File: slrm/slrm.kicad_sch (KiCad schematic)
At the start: 8 parts, among them J1 Conn_01x07, J2 Conn_01x03, J3 Conn_01x08, U1 74HCT04, U2 74HCT574, U3 IS62C256AL-45ULI

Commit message: more schematic work, ground inputs, find the footprint for the sram
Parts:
- added C1: C_Small, symbol Device:C_Small
- added unit 4 of U1
- added unit 2 of U1
- added unit 5 of U1
- added unit 6 of U1
- added unit 7 of U1
- added unit 3 of U1
- renumbered C1 to C2, C2 to C3
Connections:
- net +5V: now also C1.1, U1.14 (VCC)
- net GND: now also U2.9 (D7), U3.1 (A14), C1.2, U1.11, U1.13, U1.3, U1.5, U1.7 (GND), U1.9
- no-connect marks 3 -> 6

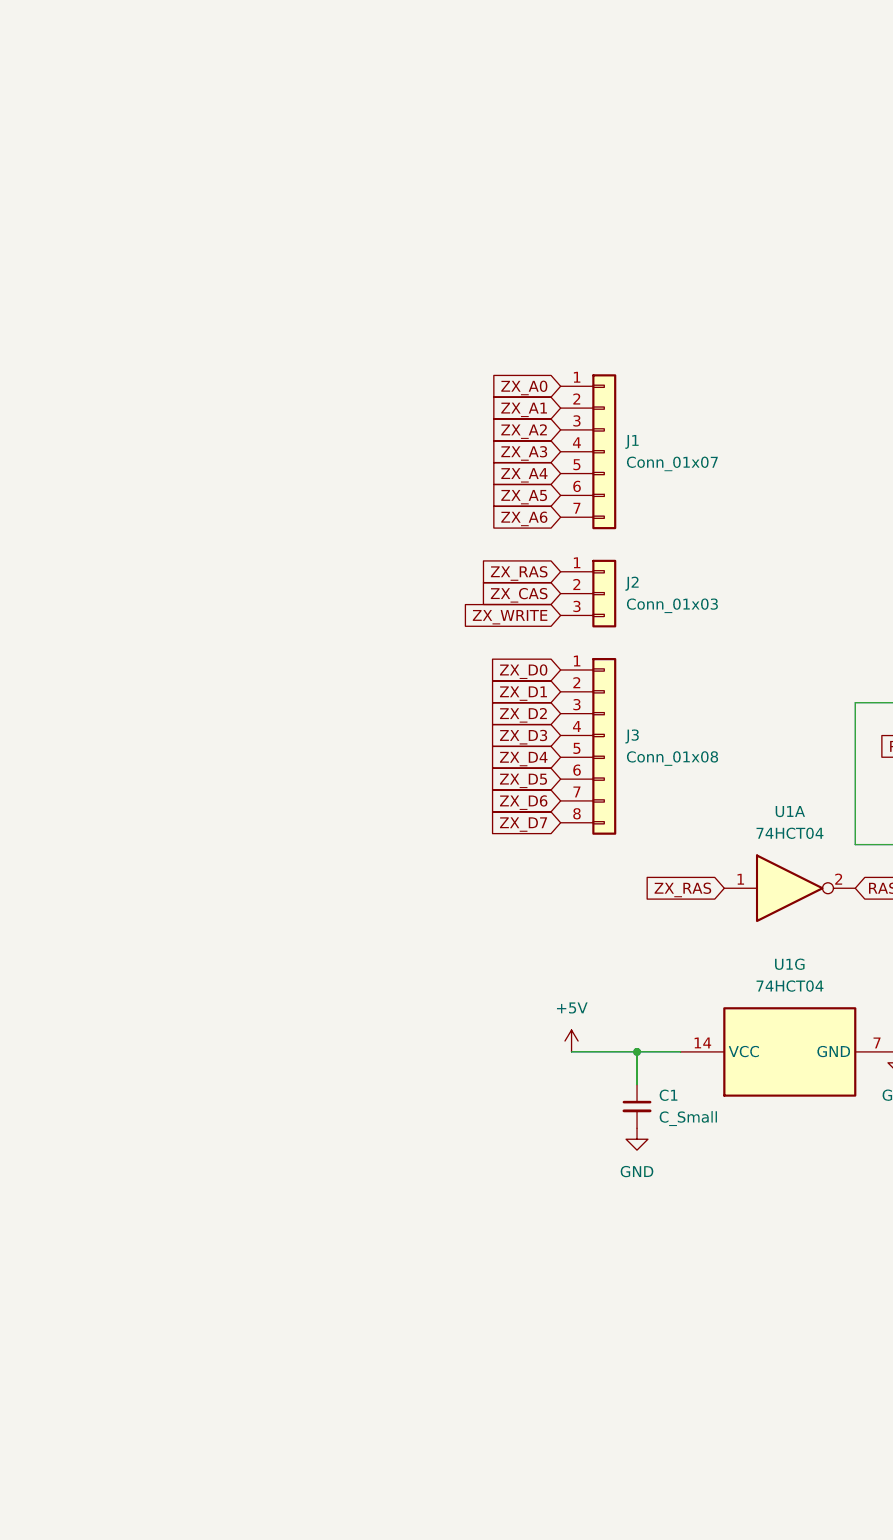
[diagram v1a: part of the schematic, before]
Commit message: split out zx connections into individual connectors, power to the inverter
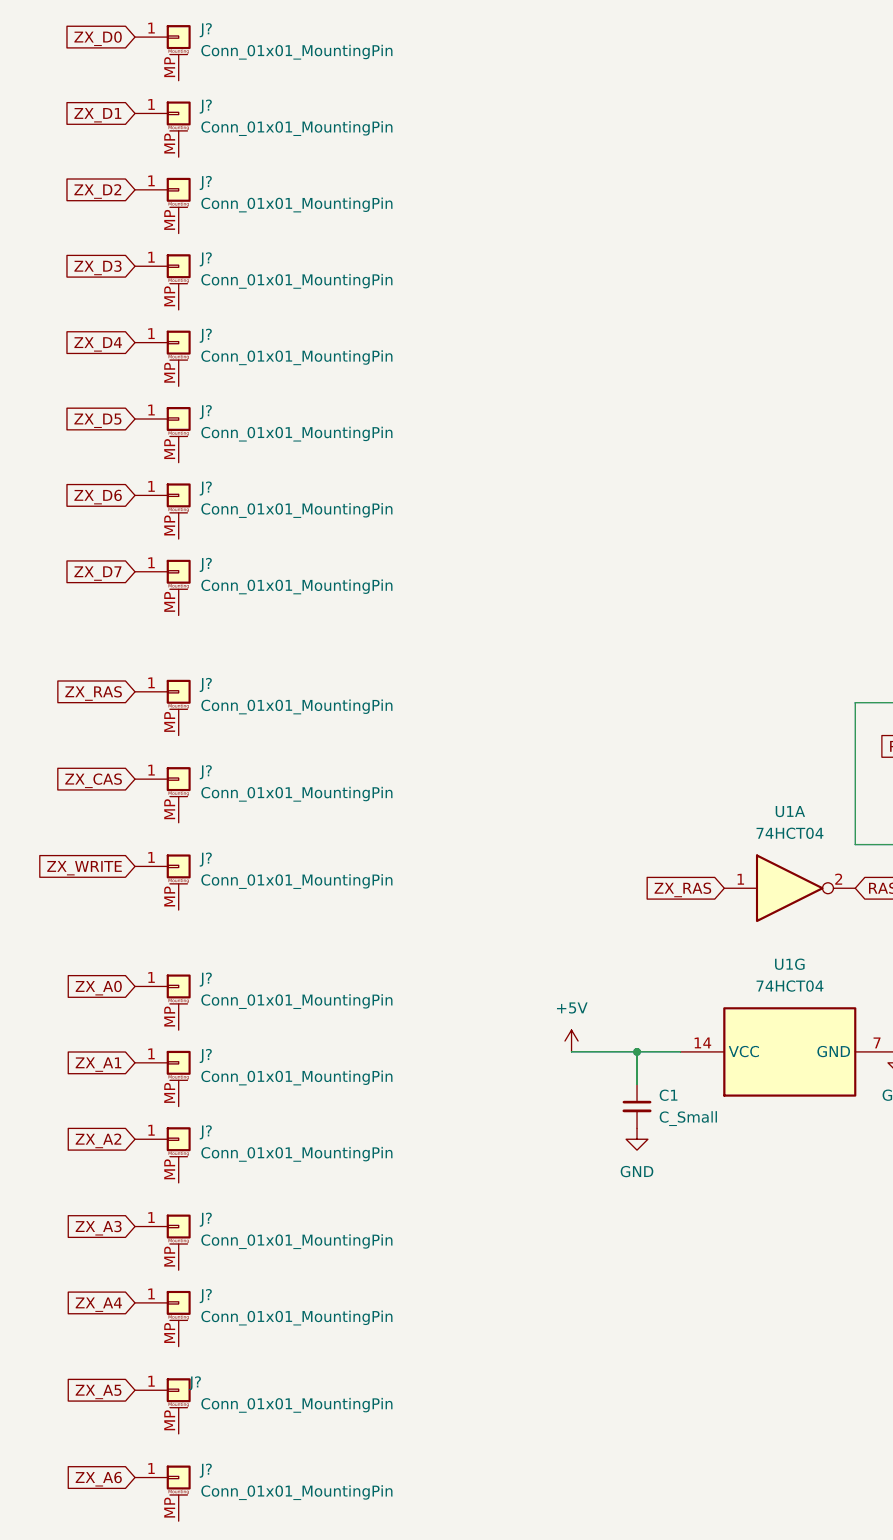
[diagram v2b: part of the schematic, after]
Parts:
- removed J1: Conn_01x07, Connector_PinHeader_1.27mm:PinHeader_1x07_P1.27mm_Vertical, symbol Connector_Generic:Conn_01x07
- removed J2: Conn_01x03, Connector_PinHeader_1.27mm:PinHeader_1x03_P1.27mm_Vertical, symbol Connector_Generic:Conn_01x03
- removed J3: Conn_01x08, Connector_PinHeader_1.27mm:PinHeader_1x08_P1.27mm_Vertical, symbol Connector_Generic:Conn_01x08
- added J? (x18): Conn_01x01_MountingPin, Connector_PinHeader_2.00mm:PinHeader_1x01_P2.00mm_Vertical, symbol Connector_Generic_MountingPin:Conn_01x01_MountingPin
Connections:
- net ZX_A0: now also J?.1 (Pin_1)
- net ZX_A1: now also J?.1 (Pin_1)
- net ZX_A2: now also J?.1 (Pin_1)
- net ZX_A3: now also J?.1 (Pin_1)
- net ZX_A4: now also J?.1 (Pin_1)
- net ZX_A5: now also J?.1 (Pin_1)
- net ZX_A6: now also J?.1 (Pin_1)
- net ZX_CAS: now also J?.1 (Pin_1)
- net ZX_D0: now also J?.1 (Pin_1)
- net ZX_D1: now also J?.1 (Pin_1)
- net ZX_D2: now also J?.1 (Pin_1)
- net ZX_D3: now also J?.1 (Pin_1)
- net ZX_D4: now also J?.1 (Pin_1)
- net ZX_D5: now also J?.1 (Pin_1)
- net ZX_D6: now also J?.1 (Pin_1)
- net ZX_D7: now also J?.1 (Pin_1)
- net ZX_RAS: now also J?.1 (Pin_1)
- net ZX_WRITE: now also J?.1 (Pin_1)

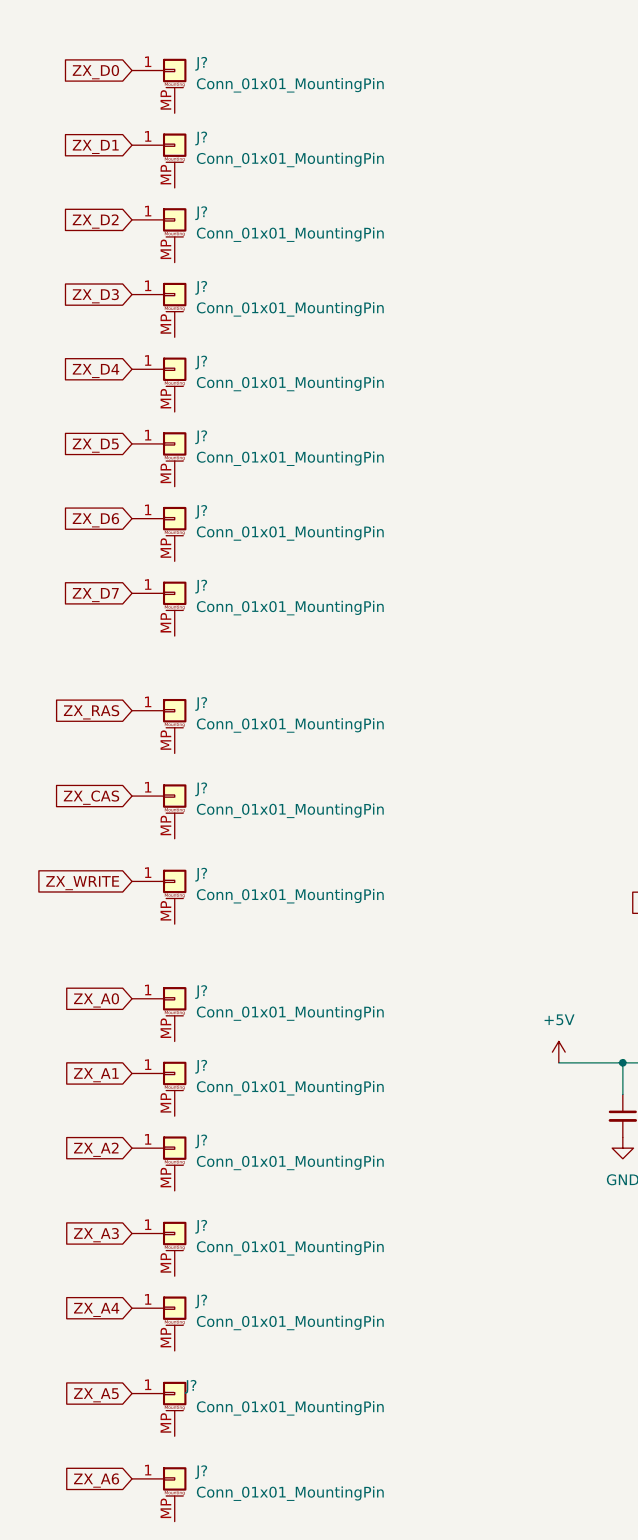
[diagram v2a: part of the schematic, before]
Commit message: use the right connectors
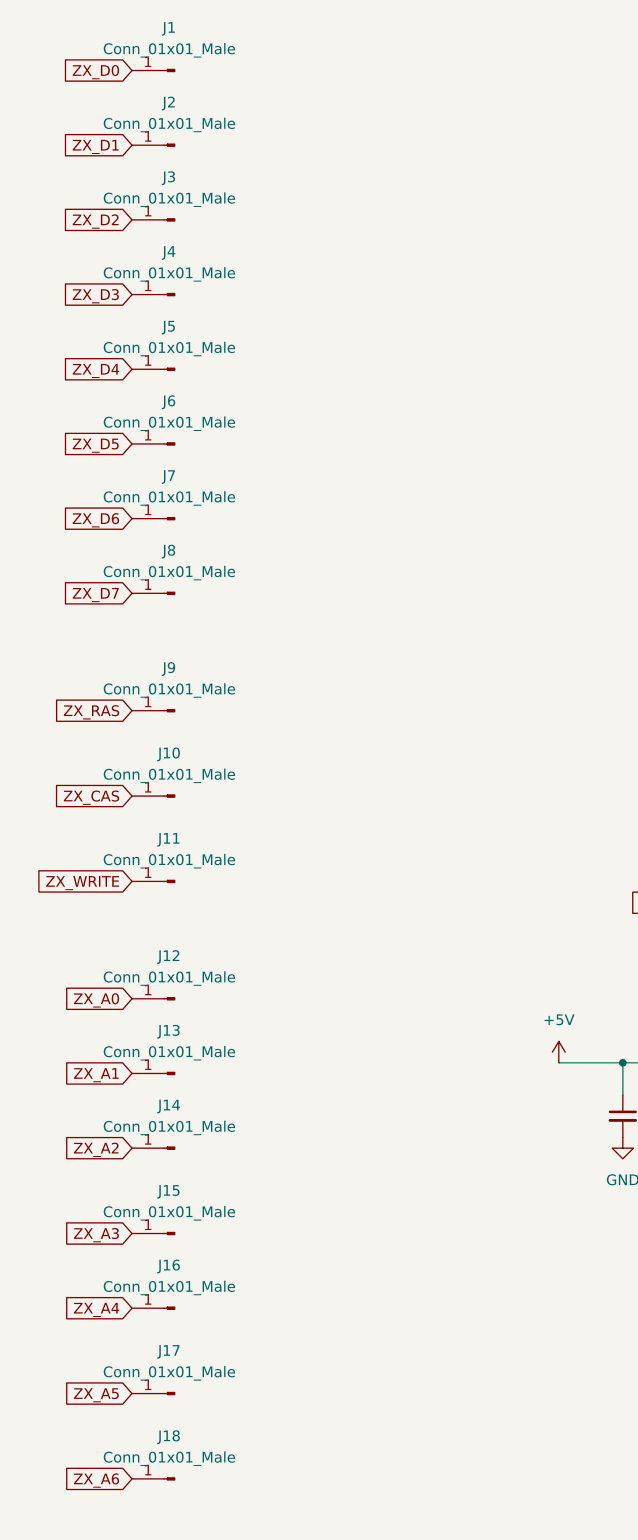
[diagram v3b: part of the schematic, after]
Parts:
- removed J? (x18): Conn_01x01_MountingPin, Connector_PinHeader_2.00mm:PinHeader_1x01_P2.00mm_Vertical, symbol Connector_Generic_MountingPin:Conn_01x01_MountingPin
- added J1, J10, J11, J12, J13, J14, J15, J16, J17, J18, J2, J3, J4, J5, J6, J7, J8, J9: Conn_01x01_Male, Connector_PinHeader_2.00mm:PinHeader_1x01_P2.00mm_Vertical, symbol Connector:Conn_01x01_Male
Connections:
- net ZX_A0: now also J12.1 (Pin_1)
- net ZX_A1: now also J13.1 (Pin_1)
- net ZX_A2: now also J14.1 (Pin_1)
- net ZX_A3: now also J15.1 (Pin_1)
- net ZX_A4: now also J16.1 (Pin_1)
- net ZX_A5: now also J17.1 (Pin_1)
- net ZX_A6: now also J18.1 (Pin_1)
- net ZX_CAS: now also J10.1 (Pin_1)
- net ZX_D0: now also J1.1 (Pin_1)
- net ZX_D1: now also J2.1 (Pin_1)
- net ZX_D2: now also J3.1 (Pin_1)
- net ZX_D3: now also J4.1 (Pin_1)
- net ZX_D4: now also J5.1 (Pin_1)
- net ZX_D5: now also J6.1 (Pin_1)
- net ZX_D6: now also J7.1 (Pin_1)
- net ZX_D7: now also J8.1 (Pin_1)
- net ZX_RAS: now also J9.1 (Pin_1)
- net ZX_WRITE: now also J11.1 (Pin_1)

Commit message: layout complete
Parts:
- removed J1, J10, J11, J12, J13, J14, J15, J16, J17, J18, J8, J9: Conn_01x01_Male, Connector_PinHeader_2.00mm:PinHeader_1x01_P2.00mm_Vertical, symbol Connector:Conn_01x01_Male
- added J1, J8: Conn_01x08_Male, Connector_PinHeader_2.54mm:PinHeader_1x08_P2.54mm_Vertical, symbol Connector:Conn_01x08_Male
- C1: footprint (none) -> Capacitor_SMD:C_1206_3216Metric
- J2: renamed from J7; value Conn_01x01_Male -> D6
- J3: renamed from J6; value Conn_01x01_Male -> D5
- J4: renamed from J5; value Conn_01x01_Male -> D4
- J5: renamed from J4; value Conn_01x01_Male -> D3
- J6: renamed from J3; value Conn_01x01_Male -> D2
- J7: renamed from J2; value Conn_01x01_Male -> D1
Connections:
- net +5V: now also J1.8 (Pin_8)
- net GND: now also J1.1 (Pin_1)
- net ZX_A0: now also J8.5 (Pin_5)
- net ZX_A1: now also J8.7 (Pin_7)
- net ZX_A2: now also J8.6 (Pin_6)
- net ZX_A3: now also J1.5 (Pin_5)
- net ZX_A4: now also J1.6 (Pin_6)
- net ZX_A5: now also J1.7 (Pin_7)
- net ZX_A6: now also J1.4 (Pin_4)
- net ZX_CAS: now also J1.2 (Pin_2)
- net ZX_D0: now also J8.2 (Pin_2)
- net ZX_D7: now also J1.3 (Pin_3)
- net ZX_RAS: now also J8.4 (Pin_4)
- net ZX_WRITE: now also J8.3 (Pin_3)
- no-connect marks 6 -> 8
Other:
- moved on the sheet: J2, J3, J4, J5, J6, J7

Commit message: work towards fab2
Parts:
- added C4: C_Small, Capacitor_THT:C_Disc_D4.3mm_W1.9mm_P5.00mm, symbol Device:C_Small
- added R1: 270R, Resistor_THT:R_Axial_DIN0207_L6.3mm_D2.5mm_P10.16mm_Horizontal, symbol Device:R
- LATCH1: renamed from U2; footprint Package_SO:SOIC-20W_7.5x12.8mm_P1.27mm -> Package_SO:SO-20_5.3x12.6mm_P1.27mm
- renumbered J7 to D1, J6 to D2, J5 to D3, J4 to D4, J3 to D5, J2 to D6, U1 to INV1, U3 to SRAM1
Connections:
- net GND: now also C4.2; no longer INV1.3, INV1.5
- net ZX_CAS: now also R1.1; no longer SRAM1.20 (~{CE})
- net INV_DELAYED_ZX_CAS: now reaches INV1.4
- net INV_DELAYED_ZX_CAS: now also INV1.5
- net DELAYED_CAS: now reaches INV1.6
- net DELAYED_CAS: now also SRAM1.20 (~{CE})
- new net DELAYED_ZX_CAS: C4.1, INV1.3, R1.2
- no-connect marks 8 -> 6
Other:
- moved on the sheet: INV1B, INV1C, INV1D, INV1E, INV1F

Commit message: version 1.2 gerbers created
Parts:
- C4: value C_Small -> C_Small, 100pF
- R1: value 270R -> 68R
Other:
- note added: "CAS delay. The SRAM doesn't hold the data for quite long enough, so this ensures CAS is delayed by a few 10s of nanoseconds, which in turn delays the removal of the data from the bus. Values worked out emprically."
- note added: "Connectors to the ZX Spectrum. 8 pin header each end and individual pins for the data lines"
- note added: "Inverter. The latch triggers on a high signal, but RAS is active low, so RAS needs inverting before going into the latch. The delayed CAS signal goes through 2 of the spare inverters to clean it up after its come out of the RC circuit. Not sure that's really necessary."
- note added: "Latch, holds the contents of the address bus when RAS comes in. That's the "row address" value. This, plus the "column address" make up the complete data address which is fed into the SRAM."
- note added: "Spare inverters, not connected."
- note added: "The SRAM, 32K device, even though 16K is all that's needed. 16K ones are rare and expensive. Triggered by (delayed) CAS, and takes the row and column addresses as input. The top half of the address space is ignored. Output is +5V and goes straight to the Spectrum's data bus."
- title: (none) -> ZX Spectrum Lower RAM Module
- moved on the sheet: C1, C2, C3, C4, INV1A, INV1B, INV1C, INV1E, INV1G, LATCH1, R1, SRAM1
